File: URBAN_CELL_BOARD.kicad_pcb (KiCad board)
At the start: 2 copper layers, 162 x 181.6 mm, 20 parts, among them J1 Conn_02x09_Odd_Even, J2 Screw_Terminal_01x01, J3 Screw_Terminal_01x01, J4 Term_01x01_M10, J5 Term_01x01_M10

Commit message: Final touches to pcb layout. Generated gerber, drill and drill map files in gerbers2.1 folder
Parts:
- moved G*** 1.25 mm to (99.0, 270.5)
- moved J5 0.92 mm to (139.9, 271.6)
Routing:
- net +48V: track 207.7 -> 202.6 mm
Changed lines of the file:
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@@
 			(psa4output no)
 			(plotreference yes)
-			(plotvalue yes)
+			(plotvalue no)
 			(plotfptext yes)
 			(plotinvisibletext no)
@@
 			(drillshape 0)
 			(scaleselection 1)
-			(outputdirectory "gerbers2.0/")
+			(outputdirectory "gerbers2.1/")
 		)
 	)
@@
 	(footprint "URBAN_CELL_CUSTOM_footprints:WURTH_M10_36PIN_TERM_7461100"
 		(layer "F.Cu")
-		(at 138.98 271.56)
+		(at 139.9 271.6)
 		(descr "<b>WP-SHFU External thread, full plain<br></b>Drill hole specification for chemical surfaces<br>Thread M10 , 36pins<br>Max Height = 24mm")
 		(property "Reference" "J5"
@@
 	(footprint "LOGO"
 		(layer "F.Cu")
-		(at 98.25 271.5)
+		(at 99 270.5)
 		(property "Reference" "G***"
 			(at 0 0 0)
@@
 	)
 	(gr_text "Sarah Qadar\nShell Eco Marathon 2023"
-		(at 98.25 277.75 0)
+		(at 98.25 276.75 0)
 		(layer "F.SilkS")
 		(effects
@@
 	)
 	(segment
-		(start 200.715 265.645)
-		(end 197.27 265.645)
+		(start 191.795 265.645)
+		(end 188 269.44)
 		(width 0.25)
 		(layer "F.Cu")
@@
 	)
 	(segment
-		(start 197.27 265.645)
-		(end 188.595 274.32)
+		(start 200.715 265.645)
+		(end 191.795 265.645)
 		(width 0.25)
 		(layer "F.Cu")
@@
 	)
 	(segment
-		(start 177.58 272)
-		(end 209.159 240.421)
-		(width 16)
+		(start 183.54 266.04)
+		(end 177.31 272.27)
+		(width 3)
 		(layer "F.Cu")
 		(net 8)
@@
 	)
 	(segment
+		(start 177.58 272)
+		(end 209.159 240.421)
+		(width 16)
+		(layer "F.Cu")
+		(net 8)
+	)
+	(segment
 		(start 166 272)
 		(end 177.58 272)
@@
 	)
 	(segment
-		(start 189.865 272.27)
+		(start 177.31 272.27)
 		(end 173.3975 272.27)
 		(width 3)

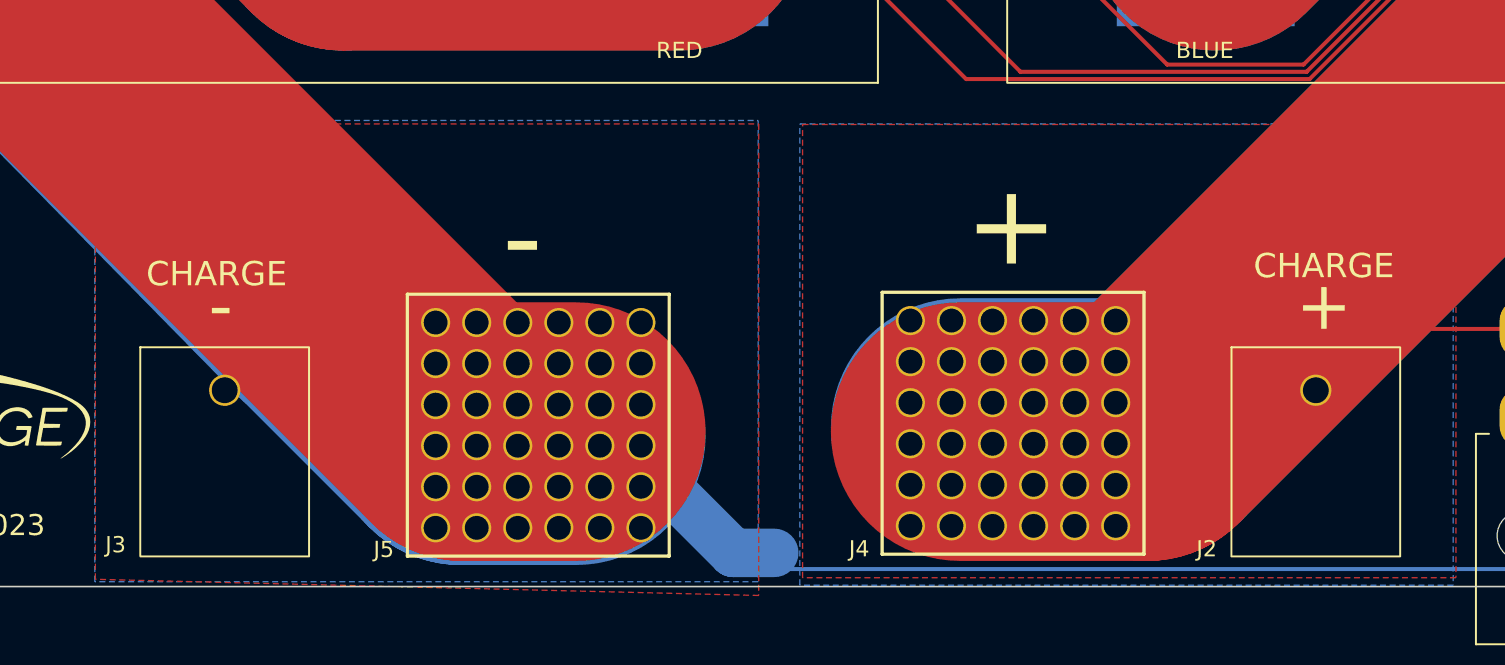
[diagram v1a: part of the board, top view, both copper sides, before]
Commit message: Replaced load and charge connectors with new parts
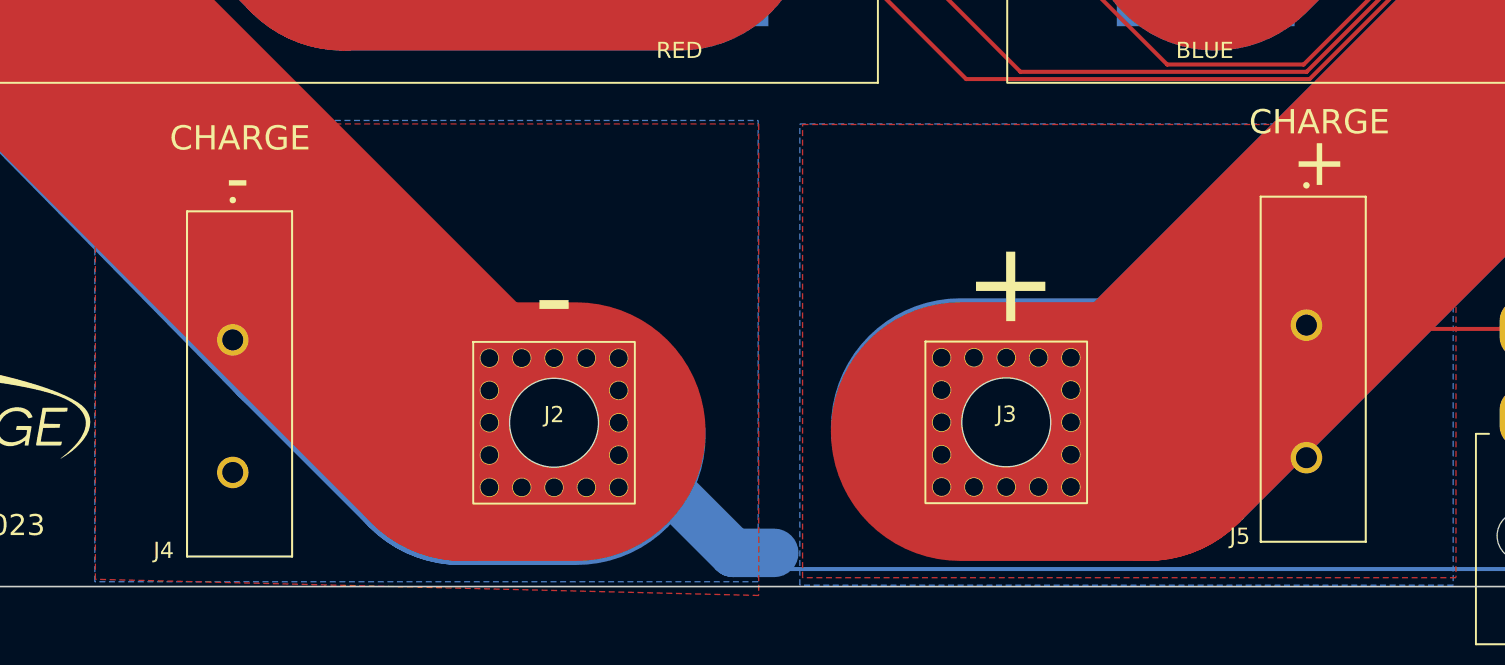
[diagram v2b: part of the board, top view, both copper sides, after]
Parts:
- J2, J3: value Screw_Terminal_01x01 -> Conn_01x01_Socket; footprint URBAN_CELL_CUSTOM_footprints:MOLEX_01X01_BARRIER_BLOCK -> URBAN_CELL_CUSTOM_footprints:AMP_01x01_WTB036SV061250R_RADSOKPOWERLOK
- J4, J5: value Term_01x01_M10 -> Conn_01x01_Socket; footprint URBAN_CELL_CUSTOM_footprints:WURTH_M10_36PIN_TERM_7461100 -> URBAN_CELL_CUSTOM_footprints:PHOENIX_01x01_1190362_TERMBLOCK_ANGLED
- moved J4 51.8 mm to (118.2, 279.7)
- moved J3 48.4 mm to (168.8, 271.4)
- moved J2 47.2 mm to (140.9, 271.4)
- moved J5 45.3 mm to (184.6, 278.8)
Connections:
- J2 pad 1: +48V -> GND
- J3 pad 1: GND -> +48V
- J4 pad 1: +48V -> GND
- J5 pad 1: GND -> +48V

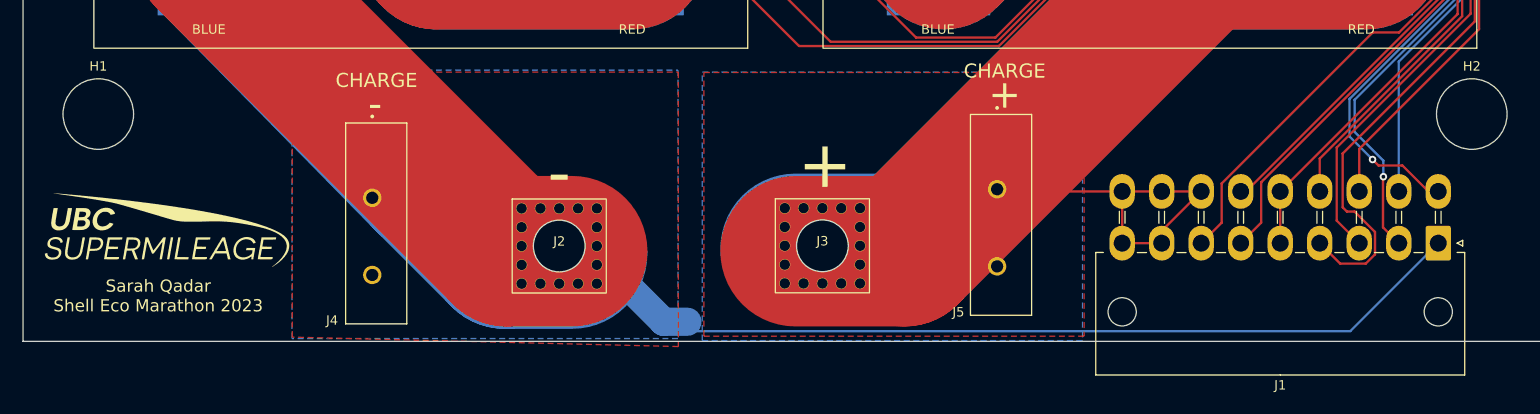
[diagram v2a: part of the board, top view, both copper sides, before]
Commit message: Added 3D models for connectors, renamed board, updated silkscreen labels, adjusted connector spacing, generated gerber, drill and drill map files
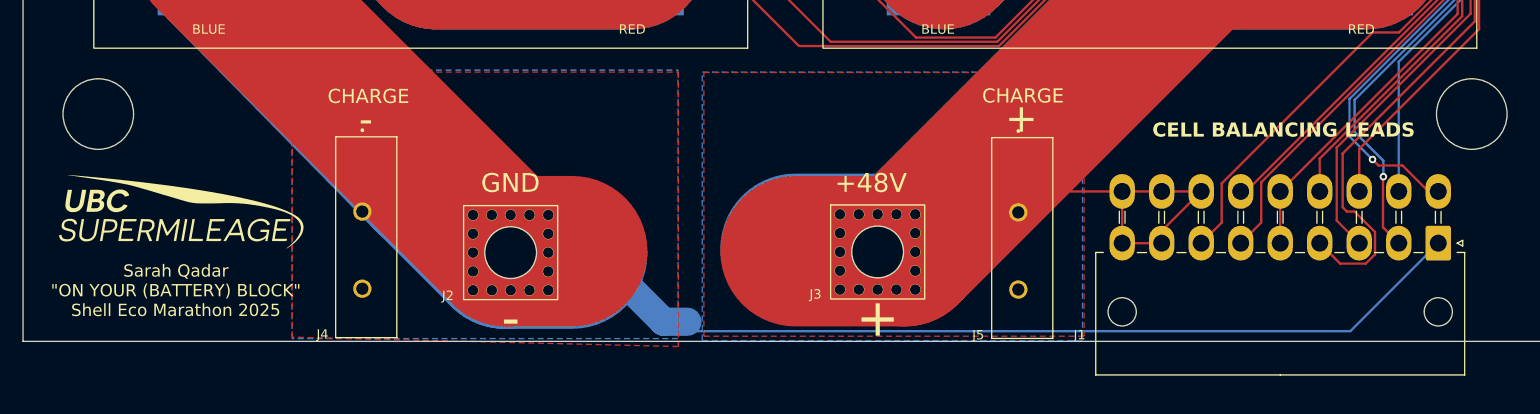
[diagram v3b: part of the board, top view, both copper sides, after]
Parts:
- moved J3 5.91 mm to (174.7, 272.1)
- moved J2 5.21 mm to (135.7, 272.1)
- moved J5 3.34 mm to (186.8, 281.3)
- moved G*** 2.46 mm to (100.5, 268.6)
- moved J4 1.80 mm to (117.1, 281.2)
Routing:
- net +48V: track 202.6 -> 193.7 mm
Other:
- board text added: "+48V"
- board text added: "CELL BALANCING LEADS"
- board text added: "GND"
- board text added: "Sarah Qadar {dblquote}ON YOUR (BATTERY) BLOCK{dblquote} Shell Eco Marathon 2025"
- board text removed: "Sarah Qadar Shell Eco Marathon 2023"
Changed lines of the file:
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@@
 			(drillshape 0)
 			(scaleselection 1)
-			(outputdirectory "gerbers2.1/")
+			(outputdirectory "gerbers2.2/")
 		)
 	)
@@
 	(footprint "URBAN_CELL_CUSTOM_footprints:PHOENIX_01x01_1190362_TERMBLOCK_ANGLED"
 		(layer "F.Cu")
-		(at 118.17 279.725)
+		(at 117.115 281.1875)
 		(property "Reference" "J4"
-			(at -1.445 -0.375 0)
+			(at -1.405 -0.3475 0)
 			(layer "F.SilkS")
 			(effects
@@
 			(solder_mask_margin 0.102)
 		)
+		(model "${KIPRJMOD}/URBAN_CELL_CUSTOM_models/PHOENIX_01x01_1190362_TERMBLOCK_ANGLED.stp"
+			(offset
+				(xyz -1.2 0 0)
+			)
+			(scale
+				(xyz 1 1 1)
+			)
+			(rotate
+				(xyz 0 0 0)
+			)
+		)
 	)
 	(footprint "Battery:Energus Li1x4pVTC6T"
@@
 	(footprint "URBAN_CELL_CUSTOM_footprints:PHOENIX_01x01_1190362_TERMBLOCK_ANGLED"
 		(layer "F.Cu")
-		(at 184.59 278.8125)
+		(at 186.845 281.275)
 		(property "Reference" "J5"
-			(at -1.29 -0.3375 0)
+			(at -1.435 -0.365 0)
 			(layer "F.SilkS")
 			(effects
@@
 			(solder_mask_margin 0.102)
 		)
+		(model "${KIPRJMOD}/URBAN_CELL_CUSTOM_models/PHOENIX_01x01_1190362_TERMBLOCK_ANGLED.stp"
+			(offset
+				(xyz -1.2 0 0)
+			)
+			(scale
+				(xyz 1 1 1)
+			)
+			(rotate
+				(xyz 0 0 0)
+			)
+		)
 	)
 	(footprint "Connector_Molex:Molex_Mini-Fit_Jr_5569-18A2_2x09_P4.20mm_Horizontal"
@@
 		(tags "connector Molex Mini-Fit_Jr top entryplastic_peg")
 		(property "Reference" "J1"
-			(at 16.8 -15.1 0)
+			(at 38.125 -9.755 0)
 			(layer "F.SilkS")
 			(effects
@@
 	(footprint "LOGO"
 		(layer "F.Cu")
-		(at 99 270.5)
+		(at 100.51 268.56)
 		(property "Reference" "G***"
 			(at 0 0 0)
@@
 		(tags "mounting hole 8.4mm no annular m8")
 		(property "Reference" "H2"
-			(at 0 -5.08 0)
-			(layer "F.SilkS")
+			(at -0.059 0.129 0)
+			(layer "F.Fab")
 			(effects
 				(font
@@
 	(footprint "URBAN_CELL_CUSTOM_footprints:AMP_01x01_WTB036SV061250R_RADSOKPOWERLOK"
 		(layer "F.Cu")
-		(at 140.875 271.45)
+		(at 135.71 272.15)
 		(property "Reference" "J2"
-			(at 0 -0.5 0)
+			(at -6.67 4.58 0)
 			(unlocked yes)
 			(layer "F.SilkS")
@@
 			(thermal_bridge_angle 90)
 		)
+		(model "${KIPRJMOD}/URBAN_CELL_CUSTOM_models/AMP_01x01_WTB036SV061250R_RADSOKPOWERLOK.stp"
+			(offset
+				(xyz -4 4 0)
+			)
+			(scale
+				(xyz 1 1 1)
+			)
+			(rotate
+				(xyz 0 0 0)
+			)
+		)
 	)
 	(footprint "Battery:Energus Li1x4pVTC6T"
@@
 	(footprint "URBAN_CELL_CUSTOM_footprints:AMP_01x01_WTB036SV061250R_RADSOKPOWERLOK"
 		(layer "F.Cu")
-		(at 168.85 271.425)
+		(at 174.72 272.08)
 		(property "Reference" "J3"
-			(at 0 -0.5 0)
+			(at -6.6 4.5 0)
 			(unlocked yes)
 			(layer "F.SilkS")
@@
 			(thermal_bridge_angle 90)
 		)
+		(model "${KIPRJMOD}/URBAN_CELL_CUSTOM_models/AMP_01x01_WTB036SV061250R_RADSOKPOWERLOK.stp"
+			(offset
+				(xyz -4 4 0)
+			)
+			(scale
+				(xyz 1 1 1)
+			)
+			(rotate
+				(xyz 0 0 0)
+			)
+		)
 	)
 	(footprint "Battery:Energus Li1x4pVTC6T"
@@
 		(tags "mounting hole 8.4mm no annular m8")
 		(property "Reference" "H1"
-			(at 0 -5.08 0)
-			(layer "F.SilkS")
+			(at -0.009 0.109 0)
+			(layer "F.Fab")
 			(effects
 				(font
@@
 	)
 	(gr_text "+"
-		(at 188.225 255.35 0)
+		(at 190 257.9 0)
 		(layer "F.SilkS")
 		(effects
@@
 		)
 	)
+	(gr_text "CELL BALANCING LEADS"
+		(at 203.91 260 0)
+		(layer "F.SilkS")
+		(effects
+			(font
+				(size 1.5 1.5)
+				(thickness 0.3)
+				(bold yes)
+			)
+			(justify left bottom)
+		)
+	)
 	(gr_text "CHARGE"
-		(at 188.225 252.85 0)
+		(at 190.175 255.5 0)
 		(layer "F.SilkS")
 		(effects
@@
 	)
 	(gr_text "-"
-		(at 140.875 263.7 0)
+		(at 135.72 279.13 0)
 		(layer "F.SilkS")
 		(effects
 			(font
-				(size 5 5)
+				(size 4 4)
 				(thickness 0.3)
 			)
@@
 	)
 	(gr_text "-"
-		(at 121.3 256.35 0)
+		(at 120.325 258 0)
 		(layer "F.SilkS")
 		(effects
@@
 		)
 	)
+	(gr_text "GND"
+		(at 132.55 265.94 0)
+		(layer "F.SilkS")
+		(effects
+			(font
+				(size 2 2)
+				(thickness 0.3)
+			)
+			(justify left bottom)
+		)
+	)
 	(gr_text "+"
-		(at 169.125 262.85 0)
+		(at 174.73 279.13 0)
 		(layer "F.SilkS")
 		(effects
 			(font
-				(size 5 5)
+				(size 4 4)
 				(thickness 0.3)
 			)
@@
 		)
 	)
-	(gr_text "Sarah Qadar\nShell Eco Marathon 2023"
-		(at 98.25 276.75 0)
+	(gr_text "Sarah Qadar\n{dblquote}ON YOUR (BATTERY) BLOCK{dblquote}\nShell Eco Marathon 2025"
+		(at 100.12 276.19 0)
 		(layer "F.SilkS")
 		(effects
@@
 	)
 	(gr_text "CHARGE"
-		(at 121.45 253.85 0)
+		(at 120.6 255.55 0)
 		(layer "F.SilkS")
 		(effects
@@
 		)
 	)
+	(gr_text "+48V"
+		(at 170.17 265.94 0)
+		(layer "F.SilkS")
+		(effects
+			(font
+				(size 2 2)
+				(thickness 0.3)
+			)
+			(justify left bottom)
+		)
+	)
 	(segment
 		(start 233.26 265.645)
@@
 		(layer "F.Cu")
 		(net 8)
-	)
-	(segment
-		(start 183.54 266.04)
-		(end 177.31 272.27)
-		(width 3)
-		(layer "F.Cu")
-		(net 8)
